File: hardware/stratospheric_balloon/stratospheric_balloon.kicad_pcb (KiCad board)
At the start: 2 copper layers, 44 parts, among them J3 SIM_Card, M1 SIM800C, Q1 Q_NPN_BCE, Q2 Q_NMOS_DGS, U1 STM32F103C8Tx, U2 LM1117-3.3, Y1 Crystal, Y2 Crystal

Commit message: Assign some footprints to sch elements
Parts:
- added J1: Conn_01x04, stratospheric_ballon:PinHeader_1x04_P2.54mm_Vertical, F.Cu at (38.1, 92.7)
- added J2: UFL, stratospheric_ballon:U.FL_Molex_MCRF_73412-0110_Vertical, F.Cu at (177.6, 110.5)
- added J4: Conn_01x03, stratospheric_ballon:PinHeader_1x03_P2.54mm_Vertical, F.Cu at (167.6, 87.6)
- added J6: Conn_01x02, Connectors_Terminal_Blocks:TerminalBlock_bornier-2_P5.08mm, F.Cu at (125.7, 55.9)
- Q2: footprint TO_SOT_Packages_SMD:TO-268-2 -> TO_SOT_Packages_SMD:SOT-23
- moved R6 37.5 mm to (87.6, 84.6), turned to 90 degrees
- moved R8 36.6 mm to (85.1, 62.2), turned to 270 degrees
- moved Q2 13.0 mm to (129.5, 63.5)
- moved R7 11.9 mm to (87.6, 62.2), turned to 270 degrees
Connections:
- J3 pad 6: Net-(J3-Pad6) -> (no net)
- M1 pad 10: Net-(M1-Pad10) -> (no net)
- M1 pad 11: Net-(M1-Pad11) -> (no net)
- M1 pad 12: Net-(M1-Pad12) -> (no net)
- M1 pad 14: Net-(M1-Pad14) -> (no net)
- M1 pad 20: Net-(M1-Pad20) -> (no net)
- M1 pad 22: Net-(M1-Pad22) -> (no net)
- M1 pad 23: Net-(M1-Pad23) -> (no net)
- M1 pad 24: Net-(M1-Pad24) -> (no net)
- M1 pad 25: Net-(M1-Pad25) -> (no net)
- M1 pad 26: Net-(M1-Pad26) -> (no net)
- M1 pad 28: Net-(M1-Pad28) -> (no net)
- M1 pad 29: Net-(M1-Pad29) -> (no net)
- M1 pad 3: Net-(M1-Pad3) -> (no net)
- M1 pad 38: Net-(M1-Pad38) -> (no net)
- M1 pad 4: Net-(M1-Pad4) -> (no net)
- M1 pad 40: Net-(M1-Pad40) -> (no net)
- M1 pad 41: Net-(M1-Pad41) -> (no net)
- M1 pad 42: Net-(M1-Pad42) -> (no net)
- M1 pad 5: Net-(M1-Pad5) -> (no net)
- M1 pad 6: Net-(M1-Pad6) -> (no net)
- M1 pad 7: Net-(M1-Pad7) -> (no net)
- M1 pad 9: Net-(M1-Pad9) -> (no net)
- U1 pad 11: Net-(U1-Pad11) -> (no net)
- U1 pad 14: /CC_NSS1 -> (no net)
- U1 pad 15: /CC_SCK1 -> (no net)
- U1 pad 17: /CC_MOSI1 -> (no net)
- U1 pad 2: Net-(U1-Pad2) -> (no net)
- U1 pad 21: /GPS_RX -> (no net)
- U1 pad 22: /GPS_TX -> (no net)
- U1 pad 25: /BME_NSS2 -> (no net)
- U1 pad 26: /BME_SCK2 -> (no net)
- U1 pad 27: /BME_MISO2 -> (no net)
- U1 pad 28: /BME_MOSI2 -> (no net)
- U1 pad 29: /MPU_INT -> (no net)
- U1 pad 32: /CC_GDO2 -> (no net)
- U1 pad 33: /CC_GDO0 -> (no net)
- U1 pad 42: /MPU_SCL1 -> (no net)
- U1 pad 43: /MPU_SDA1 -> (no net)
- U1 pad 45: /SCL1 -> (no net)
- U1 pad 46: /SDA1 -> (no net)
- XS1 pad 1: Net-(XS1-Pad1) -> (no net)
- XS1 pad 8: Net-(XS1-Pad8) -> (no net)
- XS1 pad 9: Net-(XS1-Pad9) -> (no net)

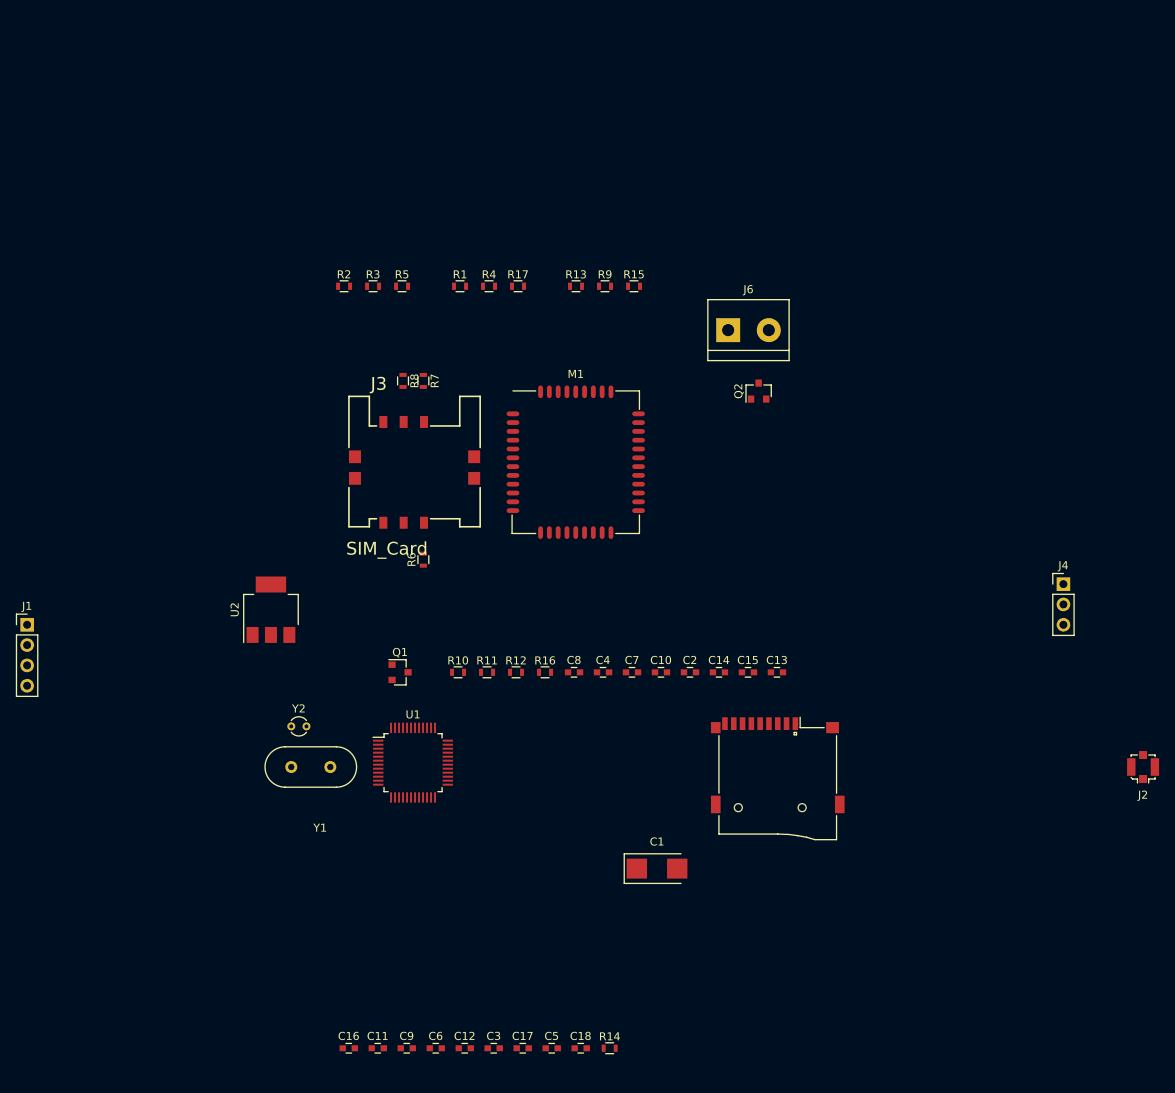
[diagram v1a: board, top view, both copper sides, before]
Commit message: Fix mistakes with footprints. Do layout
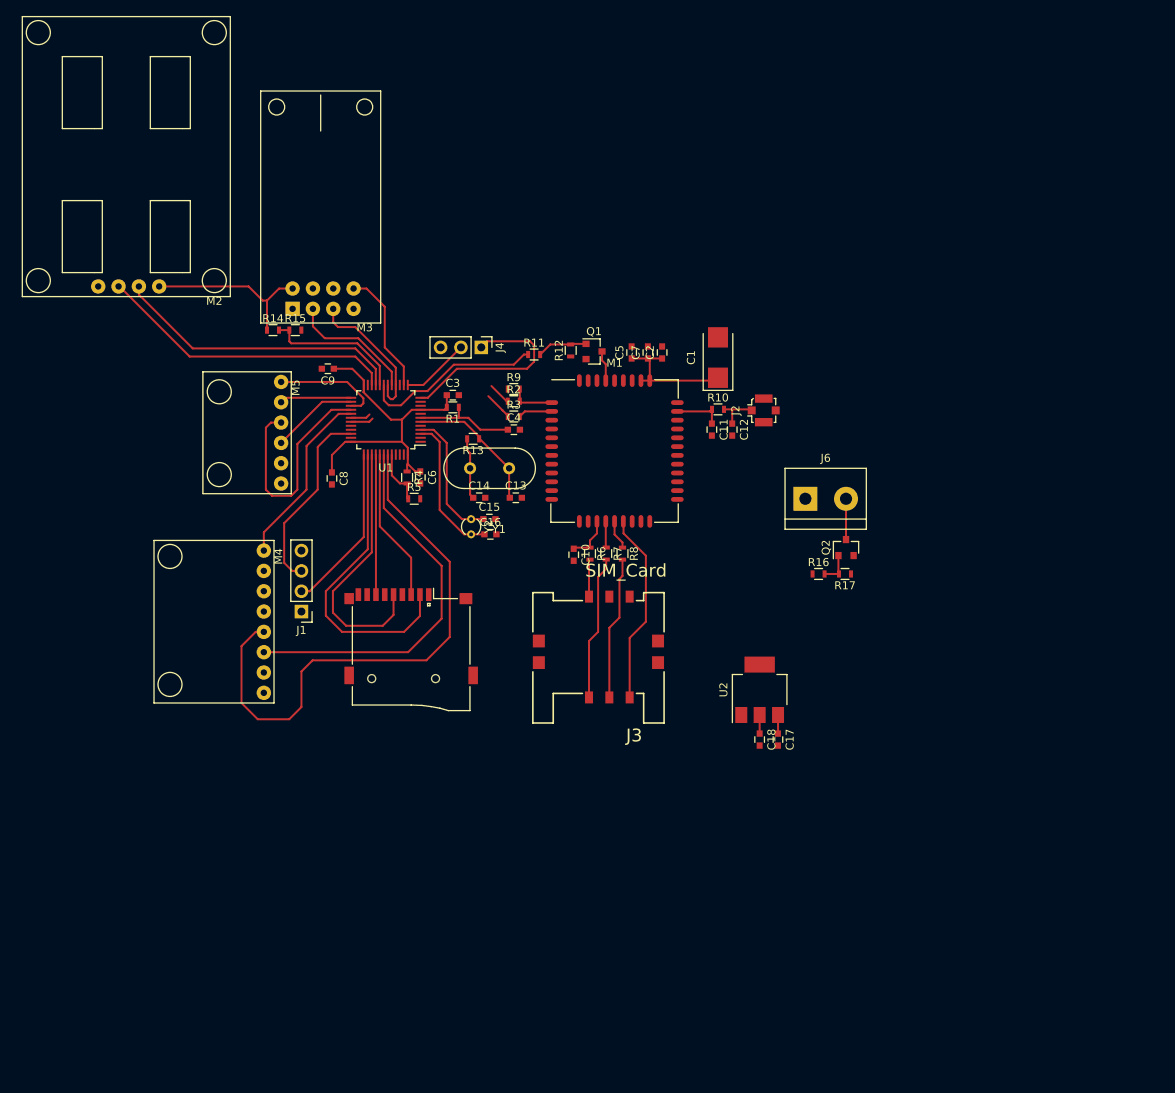
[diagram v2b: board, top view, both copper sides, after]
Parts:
- added M2: GY-GPS6MV2, stratospheric_ballon:GY-GPS6MV2_MODULE, F.Cu at (63.5, 51.7)
- added M3: CC1101_MODULE_MIDDLE, stratospheric_ballon:CC1101_MODULE_MIDDLE, F.Cu at (82.3, 55.0)
- added M4: MPU6050_MODULE, stratospheric_ballon:MPU6050_MODULE, F.Cu at (69.0, 82.2)
- added M5: BME280_MODULE, stratospheric_ballon:BME280_MODULE, F.Cu at (71.1, 61.1)
- Q1: value Q_NPN_BCE -> Q_NPN_BEC
- Q2: value Q_NMOS_DGS -> Q_NMOS_GSD
- moved R14 99.1 mm to (68.8, 55.9)
- moved C11 87.9 mm to (123.7, 68.3), turned to 270 degrees
- moved C5 87.5 mm to (113.7, 58.7), turned to 90 degrees
- moved C9 85.5 mm to (75.7, 60.7), turned to 180 degrees
- moved C12 84.2 mm to (126.2, 68.3), turned to 270 degrees
- moved C3 81.8 mm to (91.3, 64.0)
- moved J4 78.6 mm to (94.9, 58.0), turned to 270 degrees
- moved C6 71.4 mm to (87.2, 74.3), turned to 270 degrees
- moved C16 66.6 mm to (96.0, 81.4)
- moved J2 65.1 mm to (130.2, 65.9), turned to 270 degrees
- moved C1 64.3 mm to (124.5, 59.3), turned to 90 degrees
- moved U2 61.9 mm to (129.7, 100.8)
- moved R17 54.4 mm to (140.3, 86.4), turned to 180 degrees
- moved C17 50.1 mm to (132.0, 107.1), turned to 270 degrees
- moved XS1 48.6 mm to (86.1, 99.4)
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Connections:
- Q1 pad 2: /GSM_PWRKEY -> GND
- Q1 pad 3: GND -> /GSM_PWRKEY
- Q2 pad 1: Net-(J6-Pad2) -> Net-(Q2-Pad1)
- Q2 pad 2: Net-(Q2-Pad2) -> GND
- Q2 pad 3: GND -> Net-(J6-Pad2)
- R16 pad 2: Net-(Q2-Pad2) -> Net-(Q2-Pad1)
- R17 pad 2: Net-(Q2-Pad2) -> Net-(Q2-Pad1)
- U1 pad 14: (no net) -> /CC_NSS1
- U1 pad 15: (no net) -> /CC_SCK1
- U1 pad 17: (no net) -> /CC_MOSI1
- U1 pad 21: (no net) -> /GPS_RX
- U1 pad 22: (no net) -> /GPS_TX
- U1 pad 25: (no net) -> /BME_NSS2
- U1 pad 26: (no net) -> /BME_SCK2
- U1 pad 27: (no net) -> /BME_MISO2
- U1 pad 28: (no net) -> /BME_MOSI2
- U1 pad 29: (no net) -> /MPU_INT
- U1 pad 32: (no net) -> /CC_GDO2
- U1 pad 33: (no net) -> /CC_GDO0
- U1 pad 42: (no net) -> /MPU_SCL1
- U1 pad 43: (no net) -> /MPU_SDA1
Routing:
- net /MPU_SDA1: track 0.00 -> 70.4 mm
- net +3V3: track 0.00 -> 64.3 mm
- net /MPU_SCL1: track 0.00 -> 47.5 mm
- net /SD_NSS: track 0.00 -> 38.4 mm
- net /GPS_TX: track 0.00 -> 37.6 mm
- net /GPS_RX: track 0.00 -> 36.5 mm
- net /SD_SCK: track 0.00 -> 33.1 mm
- net /BME_MOSI2: track 0.00 -> 28.7 mm
- net /CON_TX: track 0.00 -> 25.5 mm
- net /GSM_SIM_VDD: track 0.00 -> 24.0 mm
- net /SWD_IO: track 0.00 -> 23.6 mm
- net /PWRKEY: track 0.00 -> 22.8 mm
- net /MPU_INT: track 0.00 -> 22.5 mm
- net /SWD_CLK: track 0.00 -> 20.9 mm
- net /SD_MOSI: track 0.00 -> 19.1 mm
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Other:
- net class Default: clearance 0.2 -> 0.25
- rule trace_clearance: 0.2 -> 0.25

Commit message: Add some changes in layout
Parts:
- moved R14 75.5 mm to (106.5, 121.3), turned to 90 degrees
- moved R15 73.2 mm to (104.5, 121.3), turned to 270 degrees
- moved M5 70.2 mm to (108.1, 120.7), turned to 0 degrees
- moved M4 67.8 mm to (124.9, 120.5), turned to 0 degrees
- moved M3 65.8 mm to (91.1, 120.2), turned to 0 degrees
- moved C9 63.6 mm to (110.6, 113.9), turned to 270 degrees
- moved R11 58.0 mm to (107.2, 116.6), turned to 270 degrees
- moved J4 55.1 mm to (92.7, 113.1), turned to 0 degrees
- moved J1 50.1 mm to (116.2, 66.8), turned to 0 degrees
- moved C3 47.7 mm to (100.8, 110.8), turned to 270 degrees
- moved U1 45.8 mm to (107.1, 106.0), turned to 0 degrees
- moved R1 45.7 mm to (98.5, 110.7), turned to 270 degrees
- moved C8 43.0 mm to (111.6, 98.9), turned to 90 degrees
- moved C4 39.5 mm to (98.5, 107.8), turned to 90 degrees
- moved Y1 35.1 mm to (94.1, 108.0), turned to 90 degrees
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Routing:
- net +3V3: track 64.3 -> 145.8 mm
- net /BURN_EN: track 0.00 -> 59.4 mm, vias 0 -> 2
- net Net-(Q1-Pad1): track 6.29 -> 63.2 mm, vias 0 -> 2
- net GND: track 0.00 -> 53.2 mm
- net /CC_GDO2: track 0.00 -> 38.0 mm, vias 0 -> 2
- net /CC_GDO0: track 0.00 -> 34.7 mm, vias 0 -> 2
- net /GPS_RX: track 36.5 -> 61.6 mm, vias 0 -> 2
- net /GSM_TX: track 5.70 -> 30.6 mm
- net /CC_SCK1: track 0.00 -> 24.8 mm
- net /GSM_RX: track 6.03 -> 29.0 mm
- net /GPS_TX: track 37.6 -> 59.4 mm, vias 0 -> 2
- net /SD_NSS: track 38.4 -> 19.2 mm
- net /MPU_SDA1: track 70.4 -> 51.6 mm, vias 0 -> 2
- net /PWRKEY: track 22.8 -> 5.54 mm
- net VBAT: track 18.8 -> 34.9 mm
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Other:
- board outline added: 61 x 79 mm

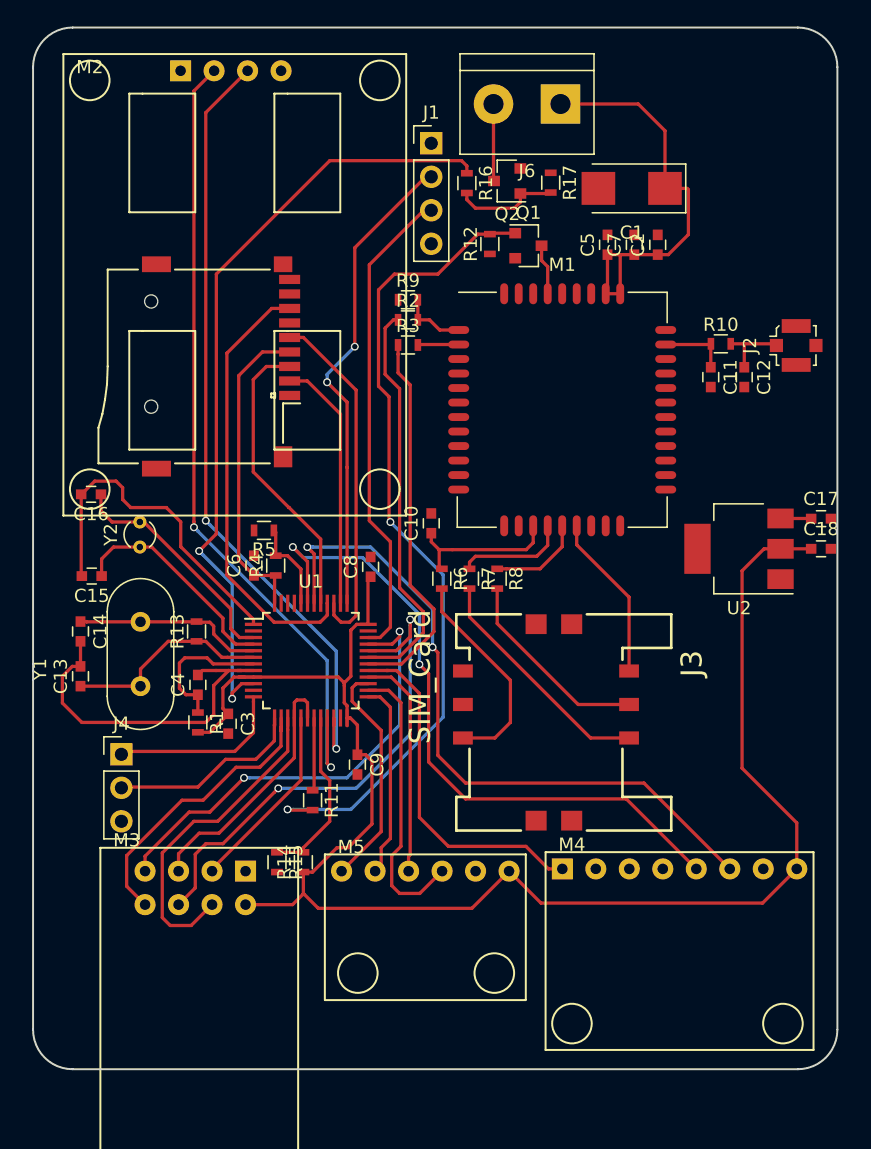
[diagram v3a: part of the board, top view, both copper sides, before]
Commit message: Change vias. Add power planes
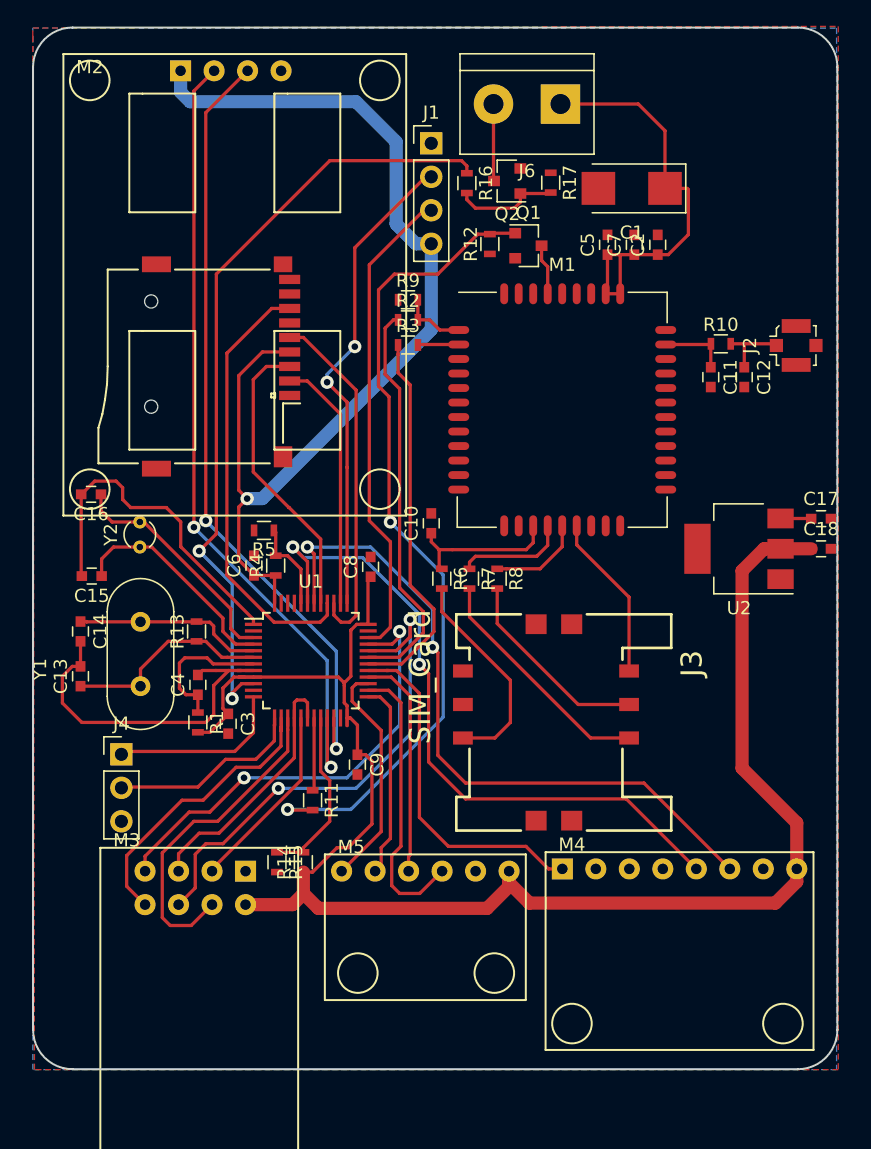
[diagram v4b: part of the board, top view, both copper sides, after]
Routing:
- net +3V3: track 145.8 -> 203.0 mm, vias 0 -> 1
- added copper zone on B.Cu, net GND
- added copper zone on F.Cu, net GND

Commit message: Add layout
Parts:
- moved U2 29.6 mm to (141.2, 68.0), turned to 0 degrees
- moved C18 23.6 mm to (141.2, 74.4), turned to 270 degrees
- moved C17 23.5 mm to (138.1, 73.0), turned to 270 degrees
- moved R16 7.40 mm to (111.7, 68.1), turned to 0 degrees
- moved C10 2.40 mm to (117.2, 97.8), turned to 180 degrees
- moved R7 2.31 mm to (121.4, 100.0)
- moved R6 2.31 mm to (119.3, 100.0)
- moved R8 2.31 mm to (123.5, 100.0)
- moved C6 1.02 mm to (102.6, 97.8)
- moved R4 1.01 mm to (104.3, 97.8)
- moved J3 1.00 mm to (125.9, 110.7)
- moved R5 0.79 mm to (103.8, 95.4)
- moved C9 0.30 mm to (110.6, 114.2), turned to 180 degrees
- moved J2 0.21 mm to (143.7, 82.0)
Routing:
- net GND: track 53.2 -> 150.6 mm, vias 0 -> 5
- net +3V3: track 203.0 -> 256.3 mm, vias 1 -> 2
- net /BURN_EN: track 59.4 -> 50.7 mm
- net Net-(Q2-Pad1): track 8.00 -> 16.6 mm
- net VBAT: track 34.9 -> 39.2 mm
- net /CC_GDO2: track 38.0 -> 41.2 mm
- net /CC_GDO0: track 34.7 -> 37.4 mm
- net Net-(C10-Pad1): track 11.7 -> 9.05 mm
- net Net-(M1-Pad16): track 8.44 -> 6.22 mm
- net /MPU_SDA1: track 51.6 -> 53.7 mm
- net /GSM_SIM_DATA: track 16.4 -> 14.2 mm
- net Net-(M1-Pad17): track 7.21 -> 5.16 mm
- net /CON_TX: track 13.4 -> 15.2 mm
- net /MPU_SCL1: track 52.9 -> 54.5 mm
- net Net-(Q1-Pad1): track 63.2 -> 64.6 mm
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
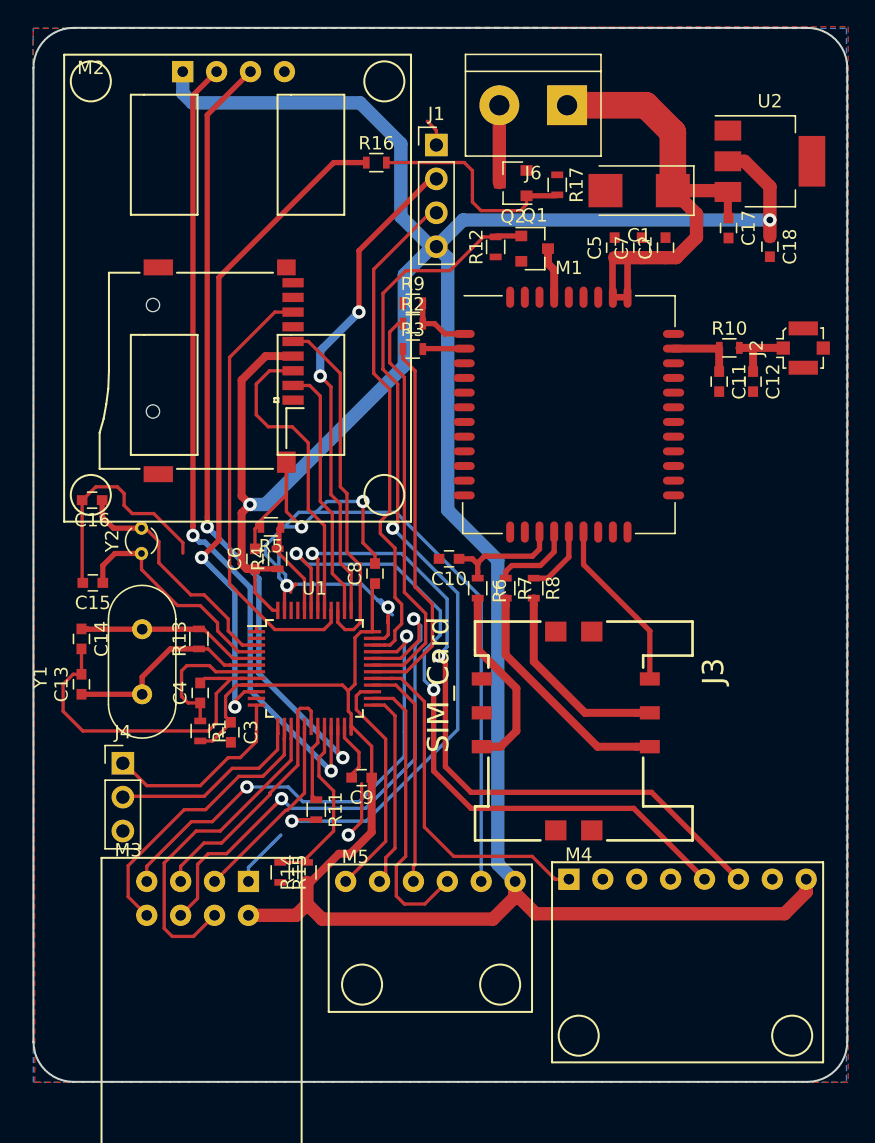
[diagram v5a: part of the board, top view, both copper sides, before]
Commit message: Add vias
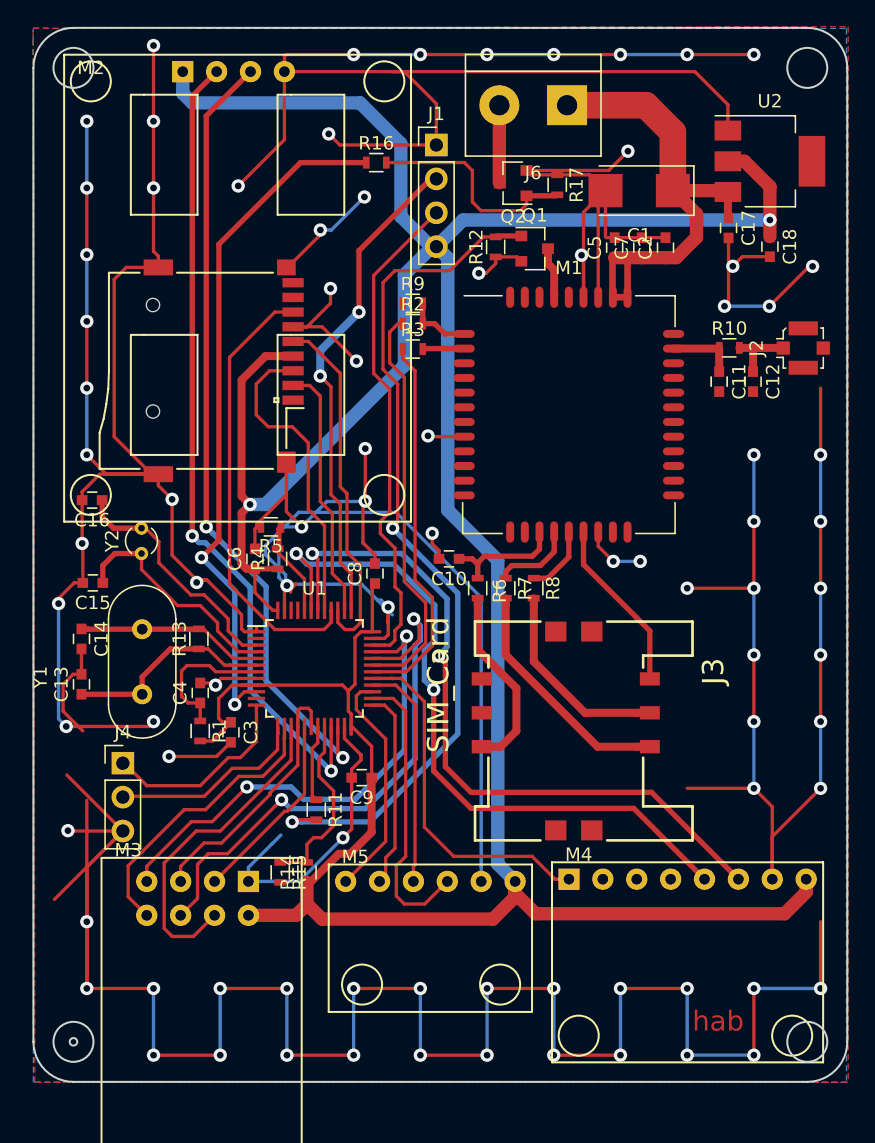
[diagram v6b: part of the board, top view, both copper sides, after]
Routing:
- net GND: track 150.6 -> 681.3 mm, vias 5 -> 84
- net /BURN_EN: track 50.7 -> 51.8 mm
- net +3V3: track 256.3 -> 257.3 mm
- net Net-(Q1-Pad1): track 64.6 -> 65.3 mm
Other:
- outline, holes or cut-outs redrawn
- rule trace_min: 0.2 -> 0.15
- board text added: "hab"
